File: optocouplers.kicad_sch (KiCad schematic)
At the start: 21 parts, among them J901 Conn_01x04, Q901 MMBT5551L, U901 EL3H7(C)(TA)-G, U902 EL3H7(C)(TA)-G

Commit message: Rename Ferrite_Bead to FerriteBead
Symbol name changed between KiCad 5 and 6...
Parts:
- FB902, FB903, FB904: symbol Device:Ferrite_Bead -> Device:FerriteBead
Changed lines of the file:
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@@
     (pin "1")
   )
-  (symbol (lib_id "Device:Ferrite_Bead") (at 179.07 43.18 270) (unit 1)
+  (symbol (lib_id "Device:FerriteBead") (at 179.07 43.18 270) (unit 1)
     (in_bom yes) (on_board yes)
     (property "Reference" "FB902" (id 0) (at 179.07 36.2204 90))
@@
     (pin "2")
   )
-  (symbol (lib_id "Device:Ferrite_Bead") (at 180.34 74.93 270) (unit 1)
+  (symbol (lib_id "Device:FerriteBead") (at 180.34 74.93 270) (unit 1)
     (in_bom yes) (on_board yes)
     (property "Reference" "FB903" (id 0) (at 180.34 67.9704 90))
@@
     (pin "2")
   )
-  (symbol (lib_id "Device:Ferrite_Bead") (at 180.34 104.14 270) (unit 1)
+  (symbol (lib_id "Device:FerriteBead") (at 180.34 104.14 270) (unit 1)
     (in_bom yes) (on_board yes)
     (property "Reference" "FB904" (id 0) (at 180.34 97.1804 90))

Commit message: Save schema with KiCad 7.0.6
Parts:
- Q901, U901, U902: JLCPCB_CORRECTION (none) -> 0;0;180

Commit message: Fix component rotations
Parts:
- J901: JLCPCB_CORRECTION (none) -> 0;3.81;90
- U901, U902: JLCPCB_CORRECTION 0;0;180 -> 0;0;270
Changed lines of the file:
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@@
       (effects (font (size 1.27 1.27)) hide)
     )
-    (property "JLCPCB_CORRECTION" "" (at 242.57 71.12 0)
+    (property "JLCPCB_CORRECTION" "0;3.81;90" (at 242.57 71.12 0)
       (effects (font (size 1.27 1.27)) hide)
     )
@@
       (effects (font (size 1.27 1.27)) hide)
     )
-    (property "JLCPCB_CORRECTION" "0;0;180" (at 86.36 60.96 0)
+    (property "JLCPCB_CORRECTION" "0;0;270" (at 86.36 60.96 0)
       (effects (font (size 1.27 1.27)) hide)
     )
@@
       (effects (font (size 1.27 1.27)) hide)
     )
-    (property "JLCPCB_CORRECTION" "0;0;180" (at 66.04 127 0)
-      (effects (font (size 1.27 1.27)) hide)
-    )
+    (property "JLCPCB_CORRECTION" "0;0;270" (at 66.04 127 0)
+      (effects (font (size 1.27 1.27)) hide)
+    )

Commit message: Change due to availability
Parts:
- J901: LCSC C358686 -> C2691448
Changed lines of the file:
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@@
       (effects (font (size 1.27 1.27)) hide)
     )
-    (property "LCSC" "C358686" (at 242.57 71.12 0)
+    (property "LCSC" "C2691448" (at 242.57 71.12 0)
       (effects (font (size 1.27 1.27)) hide)
     )

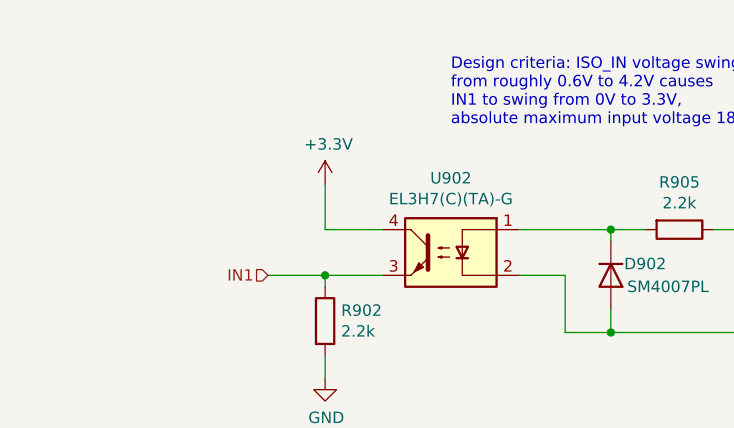
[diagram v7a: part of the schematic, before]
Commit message: Go back to ISO1050 for CAN transceiver
Also add CAN RX and TX LEDs and beef up buck capacitors
as much as space allows.
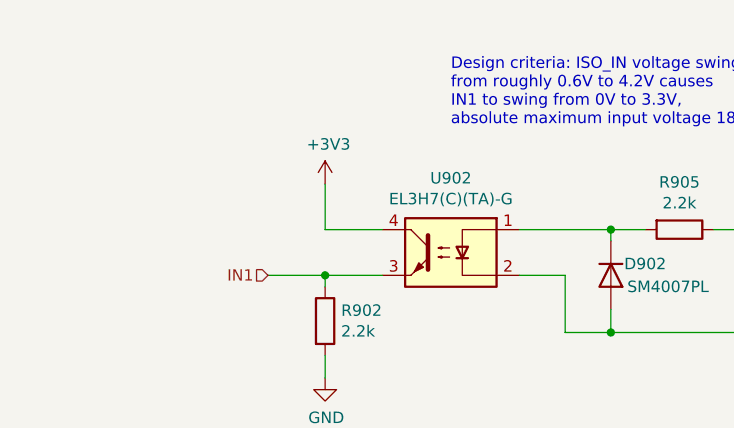
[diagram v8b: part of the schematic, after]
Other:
- company: Hat Labs Ltd -> Hat Labs Oy
- title: Sailor Hat with ESP32 -> SH-ESP32
